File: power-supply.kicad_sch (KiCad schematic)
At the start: 65 parts, among them U4 MPM54304GMN, U7 MPM3650GQW-Z

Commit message: Replaced 3V3 DC-DC with secondd MPM54304GMN, add power supply sequencing, add compatibility with CW310 signalling, add MGTAVTT LDO, add flexible FB options
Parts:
- removed C162, C163: C_22u_0805_25V, antmicro-footprints:0805-cap, symbol antmicroCapacitorsmisc:C_22u_0805_25V
- removed C164, C165: C_100n_0402, antmicro-footprints:0402-cap, symbol antmicroCapacitors0402:C_100n_0402
- removed C166, C167, C168, C169: C_22u_0603, antmicro-footprints:0603-cap, symbol antmicroCapacitors0603:C_22u_0603
- removed C170: C_39p_0402, antmicro-footprints:0402-cap, symbol antmicroCapacitors0402:C_39p_0402
- removed R56: R_20k_0402, antmicro-footprints:0402-res, symbol antmicroResistors0402:R_20k_0402
- removed R57: R_4k42_0402, antmicro-footprints:0402-res, symbol antmicroResistors0402:R_4k42_0402
- removed R?: R_470k_0402, antmicro-footprints:0402-res, symbol antmicroResistors0402:R_470k_0402
- removed U7: MPM3650GQW-Z, antmicro-footprints:MPS_QFN24, symbol antmicroPMICVoltageRegulatorsDCDCSwitchingRegulators:MPM3650GQW-Z
- added C? (x6): C_22u_0603, antmicro-footprints:0603-cap, symbol antmicroCapacitors0603:C_22u_0603
- added C? (x2): C_100n_0402, antmicro-footprints:0402-cap, symbol antmicroCapacitors0402:C_100n_0402
- added C?: C_1u_0402, data-center-dram-tester-footprints:0402-cap, symbol data-center-dram-tester:C_1u_0402
- added C? (x4): C_1u_0402, antmicro-footprints:0402-cap, symbol antmicroCapacitors0402:C_1u_0402
- added C?: C_10u_0402, antmicro-footprints:0402-cap, symbol antmicroCapacitors0402:C_10u_0402
- added C? (x2): C_22u_0805_25V, antmicro-footprints:0805-cap, symbol antmicroCapacitorsmisc:C_22u_0805_25V
- added C?: C_1u_0402_16V, antmicro-footprints:0402-cap, symbol antmicroCapacitors0402:C_1u_0402_16V
- added R? (x25): R_0R_0402, antmicro-footprints:0402-res, symbol antmicroResistors0402:R_0R_0402
- added R? (x5): R_0R_0805, antmicro-footprints:0805-res, symbol antmicroResistorsmisc:R_0R_0805
- added R? (x3): R_47k_0402, antmicro-footprints:0402-res, symbol antmicroResistors0402:R_47k_0402
- added U?: NCV8187AMT120TAG, antmicro-footprints:WSON6_TI_2x2mm, symbol antmicroPMICVoltageRegulatorsLinear:NCV8187AMT120TAG
- added U?: NCP718ASN500T1G, antmicro-footprints:SOT-23-5, symbol antmicroPMICVoltageRegulatorsLinear:NCP718ASN500T1G
- added U?: NCP451AFCT2G, antmicro-footprints:Onsemi_WLCSP6_1.40x0.90, symbol antmicroPMICPowerDistributionSwitchesLoadDrivers:NCP451AFCT2G
- added U?: LM3880, antmicro-footprints:SOT-23-6, symbol antmicroPMICPowerSequencers:LM3880
- added U?: MPM54304GMN, antmicro-footprints:MPS_LGA-33, symbol antmicroPMICVoltageRegulatorsDCDCSwitchingRegulators:MPM54304GMN
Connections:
- net +1V2: now also R43.2, R?.2; no longer R42.2
- net +1V35: now also C?.1, R?.2, U?.A1 (OUT), U?.B1 (OUT); no longer R43.2
- net +1V8: now also R42.2, R?.2; no longer R41.2
- net +3V3: now also R?.2, R?.2, R?.2, R?.2
- net GND: now also C?.2, C?.2, C?.2, C?.2, C?.2, C?.2, C?.2, C?.2, C?.2, C?.2, C?.2, C?.2, C?.2, C?.2, C?.2, C?.2, C?.2, C?.2, R?.1, R?.1, R?.1, R?.1, R?.1, R?.1, R?.1, R?.1, U?.10 (GND), U?.13 (GND), U?.16 (GND), U?.17 (SGND1), U?.2 (GND), U?.2 (GND), U?.2 (GND), U?.20 (GND), U?.21 (GND), U?.27 (GND), U?.3 (GND), U?.30 (SGND2), U?.33 (GND), U?.5 (GND), U?.7 (EP), U?.7 (GND), U?.C1 (GND)
- net MGTAVCC: now also R41.2, R?.2; no longer R44.2
- net SCL_3V3: now also U?.4 (SCL)
- net SDA_3V3: now also U?.3 (SDA)
- net VIN: now also C?.1, C?.1, C?.1, U?.1 (VIN), U?.28 (VIN), U?.29 (VIN), U?.3 (EN)
- net VOUT1: now also C?.1, C?.1, R?.1, R?.2, R?.2, U?.14 (VOUT1), U?.15 (VOUT1); no longer U4.18 (FB1)
- net VOUT2: now also C?.1, C?.1, R?.1, R?.2, R?.2, U?.8 (VOUT2), U?.9 (VOUT2); no longer U4.6 (FB2)
- net VDDR_PGOOD: now reaches U?.9 (PGOOD)
- net EN1: now reaches U?.5 (EN)
- net EN1: now also R?.1, U?.6 (FLAG1)
- net 1V2_local: now reaches C61.1, R43.1, U4.1 (VOUT3), U4.32 (VOUT3)
- net 1V2_local: now also R?.2; no longer U4.31 (FB3)
- net EN2: now reaches U4.19 (EN/SYNCI)
- net EN2: now also R?.1, U?.5 (FLAG2)
- net VOUT4 renamed IN
- net IN: now also C?.1, C?.1, R?.1, R?.2, U?.22 (VOUT4), U?.23 (VOUT4), U?.A2 (IN), U?.B2 (IN); no longer U4.24 (FB4)
- new net: C?.1, R?.1, U?.3 (EN)
- new net: C?.1, R?.1, U?.5 (SNS), U?.6 (OUT)
- new net: C?.2, C?.2
- new net: C?.1, U?.25 (VCC)
- new net +5V: R?.2, R?.2, R?.2
- new net 1V7: C?.1, R44.2, U?.1 (IN), U?.2 (EN)
- new net 5V_ALWAYS_ON: C?.1, C?.1, R?.2, R?.2, R?.2, U?.1 (VCC), U?.5 (VOUT)
- new net 5V_local: C?.1, R?.1, R?.2, R?.2, U?.1 (VOUT3), U?.32 (VOUT3)
- new net EN3: R?.1, U?.19 (EN/SYNCI), U?.4 (FLAG3)
- new net FB1: R?.1, R?.1, R?.2, U4.18 (FB1)
- new net FB2: R?.1, R?.1, R?.2, U4.6 (FB2)
- new net FB3: R?.1, R?.1, R?.2, U4.31 (FB3)
- new net FB4: R?.1, R?.2, U4.24 (FB4)
- new net FB5: R?.1, R?.1, R?.2, R?.2, U?.18 (FB1)
- new net FB6: R?.1, R?.1, R?.1, R?.2, U?.6 (FB2)
- new net FB7: R?.1, R?.1, R?.1, R?.1, R?.2, R?.2, U?.31 (FB3)
- new net FB8: U?.24 (FB4)
- new net MGTAVTT: R?.2
- new net SW_STATE: R?.2
- new net VDDR_ENABLE: U?.C2 (EN)
- no-connect marks 9 -> 8
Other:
- note added: "+1V2"
- note added: "+1V35"
- note added: "+1V8"
- note added: "+3V3"
- note added: "+5V"
- note added: "1 2 3 4"
- note added: "1V0"
- note added: "1V2 Low noise"
- note added: "1V25"
- note added: "1V85"
- note added: "Default I2C voltage set"
- note added: "Dual phase"
- note added: "Footprint for external divider operation"
- note added: "Load switch"
- note added: "Low noise LDO"
- note added: "MGTAVCC"
- note added: "MGTAVTT"
- note added: "Mount for CW310 compatibility"
- note added: "Remote sense"
- note added: "Set to ~1V7"
- note added: "Soft start delay time slot"
- note added: "X"
- note added: "connnect sense close to FPGA"
- note added: "~20ms"
- moved on the sheet: C54, C55, C56, C57, C58, C59, C60, C61, C62, C?, D?, FB?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

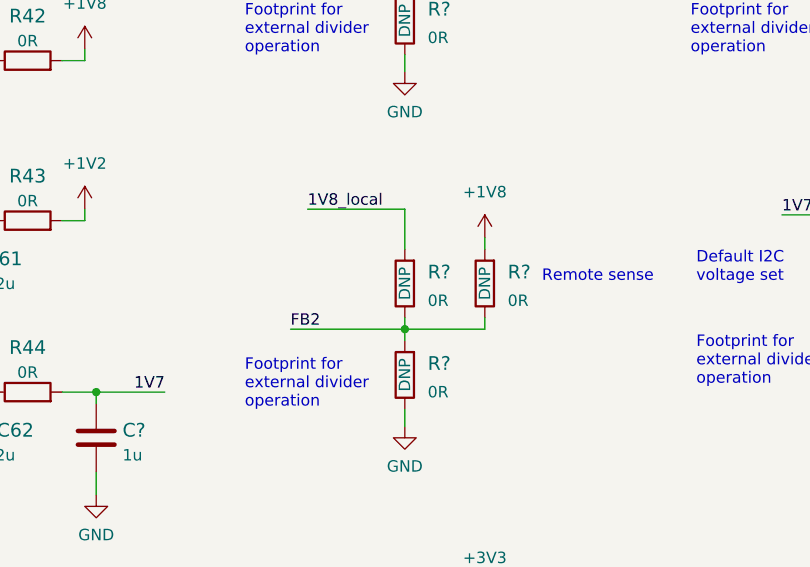
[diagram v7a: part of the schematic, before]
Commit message: Fix 1V8 DC-DC feedback, re-add FMC+ connector sheet
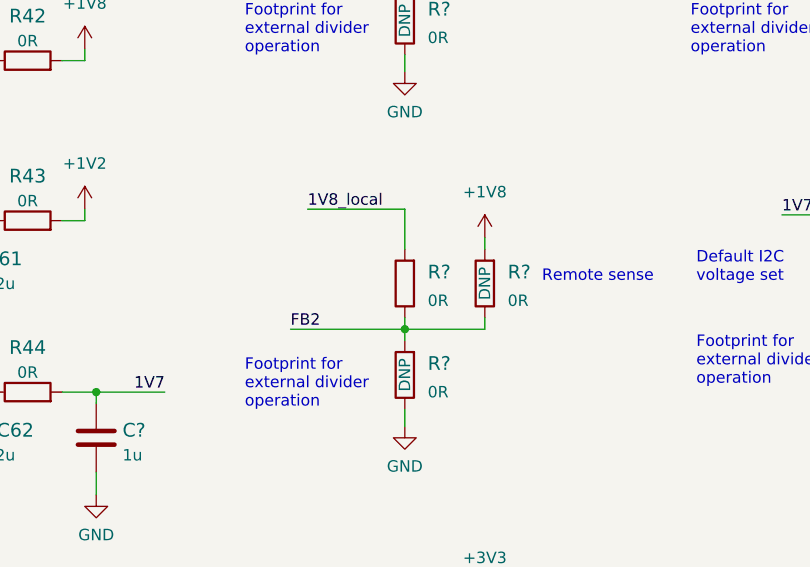
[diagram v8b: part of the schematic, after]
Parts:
- removed R?: R_0R_0402, antmicro-footprints:0402-res, symbol antmicroResistors0402:R_0R_0402
- added R?: R_0R_0402, antmicro-footprints:0402-res, symbol antmicroResistors0402:R_0R_0402
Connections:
- net FB2: now also R?.1
- net VOUT2: now also R?.2
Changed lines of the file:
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@@
     (stroke (width 0) (type default) (color 0 0 0 0))
   )
-  (wire (pts (xy 140.97 132.08) (xy 140.97 136.525))
-    (stroke (width 0) (type default) (color 0 0 0 0))
-  )
   (polyline (pts (xy 74.93 260.35) (xy 74.93 252.73))
     (stroke (width 0) (type default) (color 0 0 0 0))
@@
     (stroke (width 0) (type default) (color 0 0 0 0))
   )
+  (wire (pts (xy 140.97 144.145) (xy 140.97 145.415))
+    (stroke (width 0) (type default) (color 0 0 0 0))
+  )
   (wire (pts (xy 381 64.77) (xy 381 63.5))
     (stroke (width 0) (type default) (color 0 0 0 0))
@@
     (stroke (width 0) (type default) (color 0 0 0 0))
   )
-  (wire (pts (xy 140.97 144.145) (xy 140.97 145.415))
-    (stroke (width 0) (type default) (color 0 0 0 0))
-  )
   (wire (pts (xy 389.89 54.61) (xy 391.16 54.61))
     (stroke (width 0) (type default) (color 0 0 0 0))
@@
     (stroke (width 0) (type default) (color 0 0 0 0))
   )
+  (wire (pts (xy 140.97 132.08) (xy 140.97 136.525))
+    (stroke (width 0) (type default) (color 0 0 0 0))
+  )
   (wire (pts (xy 306.07 215.9) (xy 306.07 217.17))
     (stroke (width 0) (type default) (color 0 0 0 0))
@@
     (pin "2")
   )
-  (symbol (lib_id "antmicroResistors0402:R_0R_0402") (at 140.97 140.335 90) (unit 1)
-    (in_bom yes) (on_board yes)
-    (property "Reference" "R?" (id 0) (at 143.51 139.065 90)
-      (effects (font (size 1.524 1.524)) (justify right))
-    )
-    (property "Value" "R_0R_0402" (id 1) (at 144.78 140.335 0)
-      (effects (font (size 1.524 1.524)) hide)
-    )
-    (property "Footprint" "antmicro-footprints:0402-res" (id 2) (at 135.89 135.255 0)
-      (effects (font (size 1.524 1.524)) (justify left) hide)
-    )
-    (property "Datasheet" "" (id 3) (at 140.97 140.335 0)
-      (effects (font (size 1.27 1.27)) hide)
-    )
-    (property "Manufacturer" "PANASONIC" (id 4) (at 130.81 135.255 0)
-      (effects (font (size 1.524 1.524)) (justify left) hide)
-    )
-    (property "MPN" "ERJ2GE0R00X" (id 5) (at 133.35 135.255 0)
-      (effects (font (size 1.524 1.524)) (justify left) hide)
-    )
-    (property "Val" "0R" (id 6) (at 143.51 142.2399 90)
-      (effects (font (size 1.27 1.27)) (justify right))
-    )
-    (property "DNP" "DNP" (id 7) (at 140.97 140.335 0))
-    (pin "1")
-    (pin "2")
-  )
   (symbol (lib_id "power:GND") (at 389.89 82.55 0) (unit 1)
     (in_bom yes) (on_board yes) (fields_autoplaced)
@@
       (effects (font (size 1.27 1.27)) (justify right))
     )
+    (pin "1")
+    (pin "2")
+  )
+  (symbol (lib_id "antmicroResistors0402:R_0R_0402") (at 140.97 140.335 90) (unit 1)
+    (in_bom yes) (on_board yes) (fields_autoplaced)
+    (property "Reference" "R?" (id 0) (at 143.51 139.065 90)
+      (effects (font (size 1.524 1.524)) (justify right))
+    )
+    (property "Value" "R_0R_0402" (id 1) (at 144.78 140.335 0)
+      (effects (font (size 1.524 1.524)) hide)
+    )
+    (property "Footprint" "antmicro-footprints:0402-res" (id 2) (at 135.89 135.255 0)
+      (effects (font (size 1.524 1.524)) (justify left) hide)
+    )
+    (property "Datasheet" "" (id 3) (at 140.97 140.335 0)
+      (effects (font (size 1.27 1.27)) hide)
+    )
+    (property "Manufacturer" "PANASONIC" (id 4) (at 130.81 135.255 0)
+      (effects (font (size 1.524 1.524)) (justify left) hide)
+    )
+    (property "MPN" "ERJ2GE0R00X" (id 5) (at 133.35 135.255 0)
+      (effects (font (size 1.524 1.524)) (justify left) hide)
+    )
+    (property "Val" "0R" (id 6) (at 143.51 142.2399 90)
+      (effects (font (size 1.27 1.27)) (justify right))
+    )
